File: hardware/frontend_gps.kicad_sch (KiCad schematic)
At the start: 11 parts

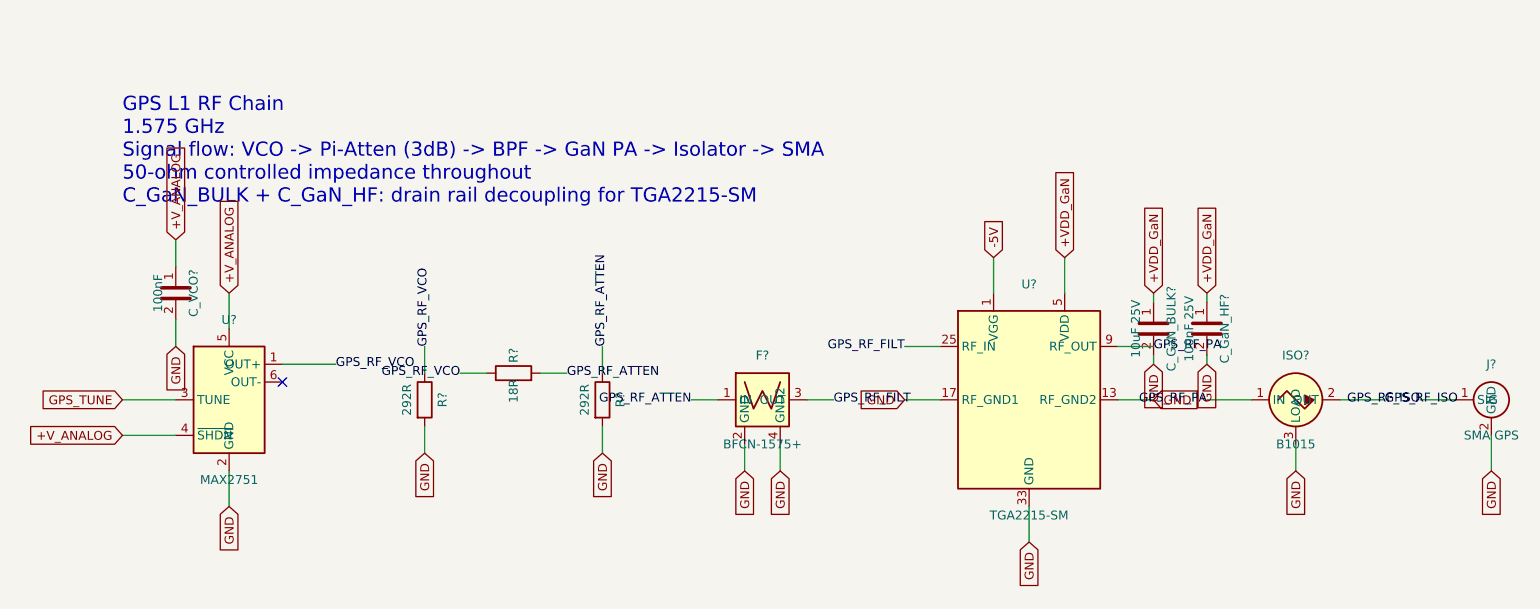
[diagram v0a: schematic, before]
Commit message: jamrf-v2: Add U3V70F15 WiFi PA regulator, FR408HR stackup, full firmware, custom footprints
- Add U3V70F15 buck-boost converter to limit WiFi PA supply to 15V (fixes ZVE-3W-83+ overvoltage)
- Update PCB stackup to Isola FR408HR (Er=3.65, tan d=0.0095) with corrected 0.40mm 50-ohm traces
- Add full operational firmware (main.py): chaos modulation engine, ST7789 display, mode control
- Add 6 custom footprints: M5StickC, Pololu D24V10F5/U3V70F15, Mini-Circuits, Wurth shield, isolator
- Add fp-lib-table and sym-lib-table for custom libraries
- Update README with logo, badges, TIIUAE disclaimer, corrected specs
- Update LICENSE with proper attribution

Co-Authored-By: Claude Opus 4.6 <noreply@anthropic.com>
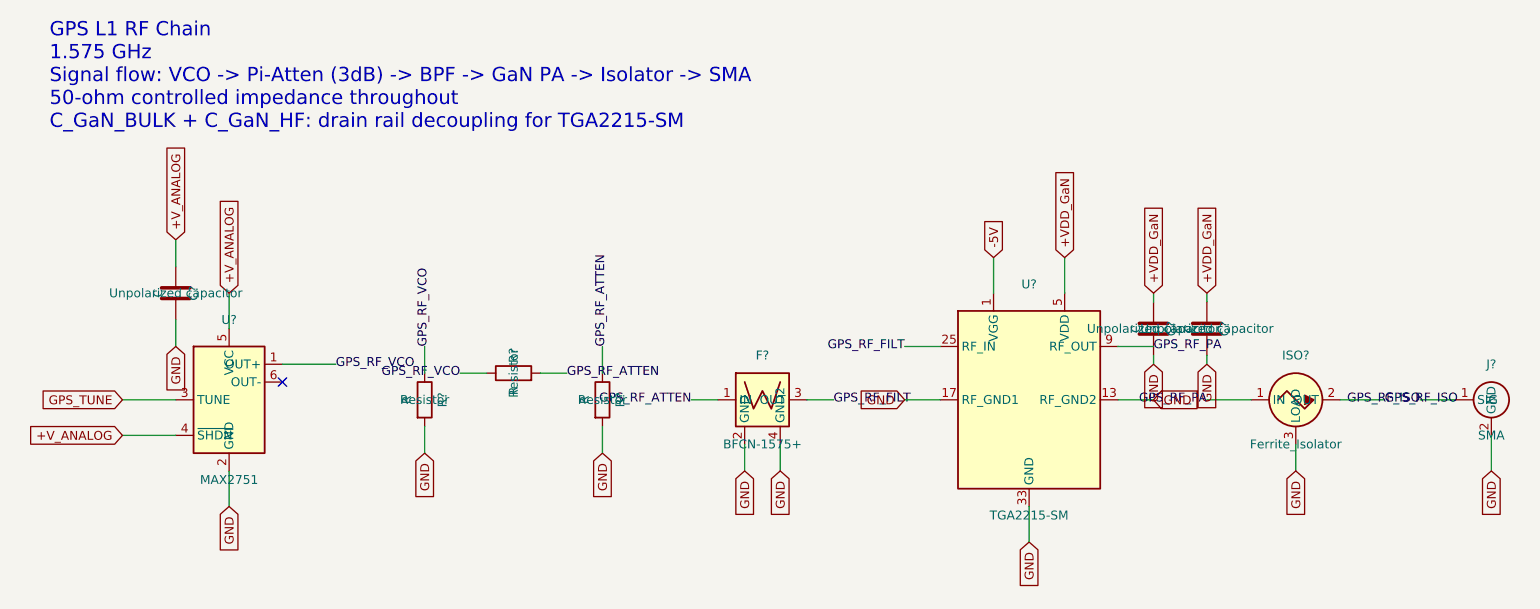
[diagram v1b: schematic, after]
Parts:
- C?: renamed from C_VCO?; value 100nF -> C
- C?: renamed from C_GaN_BULK?; value 10uF 25V -> C
- C?: renamed from C_GaN_HF?; value 100nF 25V -> C
- ISO?: value B1015 -> Ferrite_Isolator
- J?: value SMA GPS -> SMA
- R? (x2): value 292R -> R
- R?: value 18R -> R
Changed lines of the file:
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@@
 	(text "GPS L1 RF Chain\n1.575 GHz\nSignal flow: VCO -> Pi-Atten (3dB) -> BPF -> GaN PA -> Isolator -> SMA\n50-ohm controlled impedance throughout\nC_GaN_BULK + C_GaN_HF: drain rail decoupling for TGA2215-SM"
 		(exclude_from_sim no)
-		(at 40.64 40.64 0)
+		(at 30.226 29.972 0)
 		(effects
 			(font
@@
 		)
 	)
+	(wire
+		(pts
+			(xy 187.96 60.96) (xy 187.96 62.23)
+		)
+		(stroke
+			(width 0)
+			(type default)
+		)
+	)
+	(wire
+		(pts
+			(xy 187.96 69.85) (xy 187.96 71.12)
+		)
+		(stroke
+			(width 0)
+			(type default)
+		)
+	)
+	(wire
+		(pts
+			(xy 195.58 60.96) (xy 195.58 62.23)
+		)
+		(stroke
+			(width 0)
+			(type default)
+		)
+	)
+	(wire
+		(pts
+			(xy 195.58 69.85) (xy 195.58 71.12)
+		)
+		(stroke
+			(width 0)
+			(type default)
+		)
+	)
 	(label "GPS_RF_VCO"
 		(at 71.12 71.12 0)
@@
 		(property "Intersheetrefs" "${INTERSHEET_REFS}"
 			(at 236.22 86.36 0)
+			(effects
+				(font
+					(size 1.27 1.27)
+				)
+				(hide yes)
+			)
+		)
+	)
+	(global_label "+VDD_GaN"
+		(shape input)
+		(at 187.96 60.96 90)
+		(effects
+			(font
+				(size 1.27 1.27)
+			)
+			(justify left)
+		)
+		(property "Intersheetrefs" "${INTERSHEET_REFS}"
+			(at 187.96 60.96 0)
+			(effects
+				(font
+					(size 1.27 1.27)
+				)
+				(hide yes)
+			)
+		)
+	)
+	(global_label "GND"
+		(shape input)
+		(at 187.96 71.12 270)
+		(effects
+			(font
+				(size 1.27 1.27)
+			)
+			(justify right)
+		)
+		(property "Intersheetrefs" "${INTERSHEET_REFS}"
+			(at 187.96 71.12 0)
+			(effects
+				(font
+					(size 1.27 1.27)
+				)
+				(hide yes)
+			)
+		)
+	)
+	(global_label "+VDD_GaN"
+		(shape input)
+		(at 195.58 60.96 90)
+		(effects
+			(font
+				(size 1.27 1.27)
+			)
+			(justify left)
+		)
+		(property "Intersheetrefs" "${INTERSHEET_REFS}"
+			(at 195.58 60.96 0)
+			(effects
+				(font
+					(size 1.27 1.27)
+				)
+				(hide yes)
+			)
+		)
+	)
+	(global_label "GND"
+		(shape input)
+		(at 195.58 71.12 270)
+		(effects
+			(font
+				(size 1.27 1.27)
+			)
+			(justify right)
+		)
+		(property "Intersheetrefs" "${INTERSHEET_REFS}"
+			(at 195.58 71.12 0)
 			(effects
 				(font
@@
 		(on_board yes)
 		(dnp no)
-		(property "Reference" "C_VCO?"
+		(property "Reference" "C?"
 			(at 50.8 60.96 90)
 			(effects
@@
 			)
 		)
-		(property "Value" "100nF"
+		(property "Value" "C"
 			(at 45.72 60.96 90)
 			(effects
@@
 			)
 		)
-		(property "Description" ""
+		(property "Description" "Unpolarized capacitor"
 			(at 48.26 60.96 0)
 			(effects
@@
 			(project "jamrf-v2"
 				(path "/b0000001-0000-0000-0000-000000000001/b0000001-0000-0000-0000-000000000020"
-					(reference "C_VCO?")
+					(reference "C?")
 					(unit 1)
 				)
@@
 			)
 		)
-		(property "Value" "292R"
+		(property "Value" "R"
 			(at 81.28 76.2 90)
 			(effects
@@
 			)
 		)
-		(property "Description" ""
+		(property "Description" "Resistor"
 			(at 83.82 76.2 0)
 			(effects
@@
 			)
 		)
-		(property "Value" "18R"
+		(property "Value" "R"
 			(at 96.52 74.93 0)
 			(effects
@@
 			)
 		)
-		(property "Description" ""
+		(property "Description" "Resistor"
 			(at 96.52 72.39 0)
 			(effects
@@
 			)
 		)
-		(property "Value" "292R"
+		(property "Value" "R"
 			(at 106.68 76.2 90)
 			(effects
@@
 			)
 		)
-		(property "Description" ""
+		(property "Description" "Resistor"
 			(at 109.22 76.2 0)
 			(effects
@@
 			)
 		)
-		(property "Value" "B1015"
+		(property "Value" "Ferrite_Isolator"
 			(at 208.28 82.55 0)
 			(effects
@@
 			)
 		)
-		(property "Value" "SMA GPS"
+		(property "Value" "SMA"
 			(at 236.22 81.28 0)
 			(effects
@@
 					(unit 1)
 				)
-			)
-		)
-	)
-	(wire
-		(pts
-			(xy 187.96 60.96) (xy 187.96 62.23)
-		)
-		(stroke
-			(width 0)
-			(type default)
-		)
-	)
-	(wire
-		(pts
-			(xy 187.96 69.85) (xy 187.96 71.12)
-		)
-		(stroke
-			(width 0)
-			(type default)
-		)
-	)
-	(wire
-		(pts
-			(xy 195.58 60.96) (xy 195.58 62.23)
-		)
-		(stroke
-			(width 0)
-			(type default)
-		)
-	)
-	(wire
-		(pts
-			(xy 195.58 69.85) (xy 195.58 71.12)
-		)
-		(stroke
-			(width 0)
-			(type default)
-		)
-	)
-	(global_label "+VDD_GaN"
-		(shape input)
-		(at 187.96 60.96 90)
-		(effects
-			(font
-				(size 1.27 1.27)
-			)
-			(justify left)
-		)
-		(property "Intersheetrefs" "${INTERSHEET_REFS}"
-			(at 187.96 60.96 0)
-			(effects
-				(font
-					(size 1.27 1.27)
-				)
-				(hide yes)
-			)
-		)
-	)
-	(global_label "GND"
-		(shape input)
-		(at 187.96 71.12 270)
-		(effects
-			(font
-				(size 1.27 1.27)
-			)
-			(justify right)
-		)
-		(property "Intersheetrefs" "${INTERSHEET_REFS}"
-			(at 187.96 71.12 0)
-			(effects
-				(font
-					(size 1.27 1.27)
-				)
-				(hide yes)
-			)
-		)
-	)
-	(global_label "+VDD_GaN"
-		(shape input)
-		(at 195.58 60.96 90)
-		(effects
-			(font
-				(size 1.27 1.27)
-			)
-			(justify left)
-		)
-		(property "Intersheetrefs" "${INTERSHEET_REFS}"
-			(at 195.58 60.96 0)
-			(effects
-				(font
-					(size 1.27 1.27)
-				)
-				(hide yes)
-			)
-		)
-	)
-	(global_label "GND"
-		(shape input)
-		(at 195.58 71.12 270)
-		(effects
-			(font
-				(size 1.27 1.27)
-			)
-			(justify right)
-		)
-		(property "Intersheetrefs" "${INTERSHEET_REFS}"
-			(at 195.58 71.12 0)
-			(effects
-				(font
-					(size 1.27 1.27)
-				)
-				(hide yes)
 			)
 		)
@@
 		(on_board yes)
 		(dnp no)
-		(property "Reference" "C_GaN_BULK?"
+		(property "Reference" "C?"
 			(at 190.5 66.04 90)
 			(effects
@@
 			)
 		)
-		(property "Value" "10uF 25V"
+		(property "Value" "C"
 			(at 185.42 66.04 90)
 			(effects
@@
 			)
 		)
-		(property "Description" ""
+		(property "Description" "Unpolarized capacitor"
 			(at 187.96 66.04 0)
 			(effects
@@
 			(project "jamrf-v2"
 				(path "/b0000001-0000-0000-0000-000000000001/b0000001-0000-0000-0000-000000000020"
-					(reference "C_GaN_BULK?")
+					(reference "C?")
 					(unit 1)
 				)
@@
 		(on_board yes)
 		(dnp no)
-		(property "Reference" "C_GaN_HF?"
+		(property "Reference" "C?"
 			(at 198.12 66.04 90)
 			(effects
@@
 			)
 		)
-		(property "Value" "100nF 25V"
+		(property "Value" "C"
 			(at 193.04 66.04 90)
 			(effects
@@
 			)
 		)
-		(property "Description" ""
+		(property "Description" "Unpolarized capacitor"
 			(at 195.58 66.04 0)
 			(effects
@@
 			(project "jamrf-v2"
 				(path "/b0000001-0000-0000-0000-000000000001/b0000001-0000-0000-0000-000000000020"
-					(reference "C_GaN_HF?")
+					(reference "C?")
 					(unit 1)
 				)

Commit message: Annotate all component references and update CLAUDE.md
- All component references annotated (U1-U10, R1-R17, C1-C19, Q1-Q4, etc.)
- Fix CLAUDE.md: correct jamrf-v4 description (dual-band, not WiFi-only)
- Update CLAUDE.md: file paths match main branch structure, add firmware docs
- Remove resolved known issues (annotation, footprint library)

Co-Authored-By: Claude Opus 4.6 <noreply@anthropic.com>
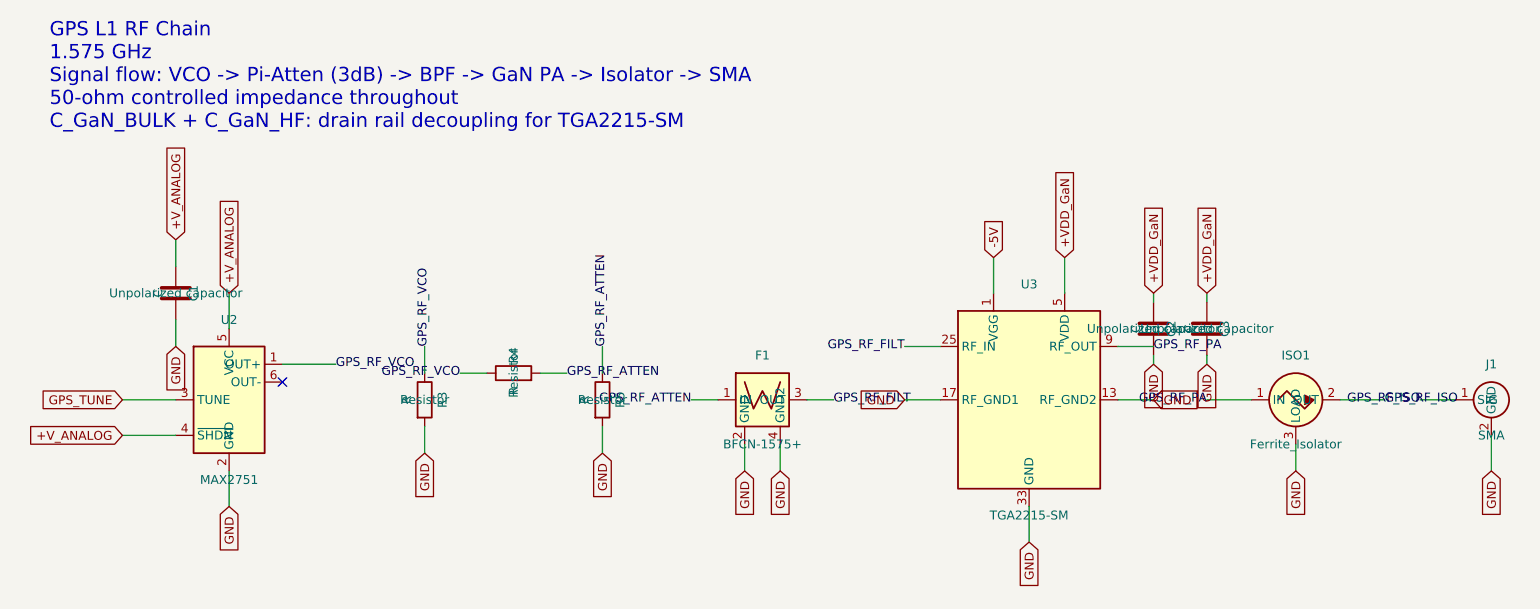
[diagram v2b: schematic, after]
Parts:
- gave numbers to parts that had none: 11
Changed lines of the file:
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@@
 		(on_board yes)
 		(dnp no)
-		(property "Reference" "U?"
+		(property "Reference" "U2"
 			(at 55.88 64.77 0)
 			(effects
@@
 			(project "jamrf-v2"
 				(path "/b0000001-0000-0000-0000-000000000001/b0000001-0000-0000-0000-000000000020"
-					(reference "U?")
+					(reference "U2")
 					(unit 1)
 				)
@@
 		(on_board yes)
 		(dnp no)
-		(property "Reference" "C?"
+		(property "Reference" "C1"
 			(at 50.8 60.96 90)
 			(effects
@@
 			(project "jamrf-v2"
 				(path "/b0000001-0000-0000-0000-000000000001/b0000001-0000-0000-0000-000000000020"
-					(reference "C?")
+					(reference "C1")
 					(unit 1)
 				)
@@
 		(on_board yes)
 		(dnp no)
-		(property "Reference" "R?"
+		(property "Reference" "R3"
 			(at 86.36 76.2 90)
 			(effects
@@
 			(project "jamrf-v2"
 				(path "/b0000001-0000-0000-0000-000000000001/b0000001-0000-0000-0000-000000000020"
-					(reference "R?")
+					(reference "R3")
 					(unit 1)
 				)
@@
 		(on_board yes)
 		(dnp no)
-		(property "Reference" "R?"
+		(property "Reference" "R4"
 			(at 96.52 69.85 0)
 			(effects
@@
 			(project "jamrf-v2"
 				(path "/b0000001-0000-0000-0000-000000000001/b0000001-0000-0000-0000-000000000020"
-					(reference "R?")
+					(reference "R4")
 					(unit 1)
 				)
@@
 		(on_board yes)
 		(dnp no)
-		(property "Reference" "R?"
+		(property "Reference" "R5"
 			(at 111.76 76.2 90)
 			(effects
@@
 			(project "jamrf-v2"
 				(path "/b0000001-0000-0000-0000-000000000001/b0000001-0000-0000-0000-000000000020"
-					(reference "R?")
+					(reference "R5")
 					(unit 1)
 				)
@@
 		(on_board yes)
 		(dnp no)
-		(property "Reference" "F?"
+		(property "Reference" "F1"
 			(at 132.08 69.85 0)
 			(effects
@@
 			(project "jamrf-v2"
 				(path "/b0000001-0000-0000-0000-000000000001/b0000001-0000-0000-0000-000000000020"
-					(reference "F?")
+					(reference "F1")
 					(unit 1)
 				)
@@
 		(on_board yes)
 		(dnp no)
-		(property "Reference" "U?"
+		(property "Reference" "U3"
 			(at 170.18 59.69 0)
 			(effects
@@
 			(project "jamrf-v2"
 				(path "/b0000001-0000-0000-0000-000000000001/b0000001-0000-0000-0000-000000000020"
-					(reference "U?")
+					(reference "U3")
 					(unit 1)
 				)
@@
 		(on_board yes)
 		(dnp no)
-		(property "Reference" "ISO?"
+		(property "Reference" "ISO1"
 			(at 208.28 69.85 0)
 			(effects
@@
 			(project "jamrf-v2"
 				(path "/b0000001-0000-0000-0000-000000000001/b0000001-0000-0000-0000-000000000020"
-					(reference "ISO?")
+					(reference "ISO1")
 					(unit 1)
 				)
@@
 		(on_board yes)
 		(dnp no)
-		(property "Reference" "J?"
+		(property "Reference" "J1"
 			(at 236.22 71.12 0)
 			(effects
@@
 			(project "jamrf-v2"
 				(path "/b0000001-0000-0000-0000-000000000001/b0000001-0000-0000-0000-000000000020"
-					(reference "J?")
+					(reference "J1")
 					(unit 1)
 				)
@@
 		(on_board yes)
 		(dnp no)
-		(property "Reference" "C?"
+		(property "Reference" "C2"
 			(at 190.5 66.04 90)
 			(effects
@@
 			(project "jamrf-v2"
 				(path "/b0000001-0000-0000-0000-000000000001/b0000001-0000-0000-0000-000000000020"
-					(reference "C?")
+					(reference "C2")
 					(unit 1)
 				)
@@
 		(on_board yes)
 		(dnp no)
-		(property "Reference" "C?"
+		(property "Reference" "C3"
 			(at 198.12 66.04 90)
 			(effects
@@
 			(project "jamrf-v2"
 				(path "/b0000001-0000-0000-0000-000000000001/b0000001-0000-0000-0000-000000000020"
-					(reference "C?")
-					(unit 1)
-				)
+					(reference "C3")
+					(unit 1)
+				)
